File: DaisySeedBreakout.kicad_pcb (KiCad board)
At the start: 4 copper layers, 39.3 x 60.7 mm, 107 parts, among them J1 Conn_01x03, J10 Conn_01x03, J11 Conn_01x02, J12 Conn_01x02, J13 Conn_01x02, J14 Conn_01x03, J15 USB_B_Micro, J16 Conn_01x02, J17 Conn_01x02, J18 Conn_02x04, J19 Conn_01x06, J2 Conn_01x02, J20 Conn_01x04, J21 Conn_02x04, J23 Pins_02x10_P2.54mm_TH, J24 Conn_01x10, J25 Conn_01x02, J26 Conn_01x02, J3 Conn_01x03, J4 5027740891, J5 Conn_01x04, J6 Conn_01x02, J7 Conn_01x04, J8 Conn_01x02, J9 Conn_01x02, U1 H11L1M, U10 TPD2EUSB30ADRTR, U2 MAX4466EXK_T, U7 TLV9062IDR

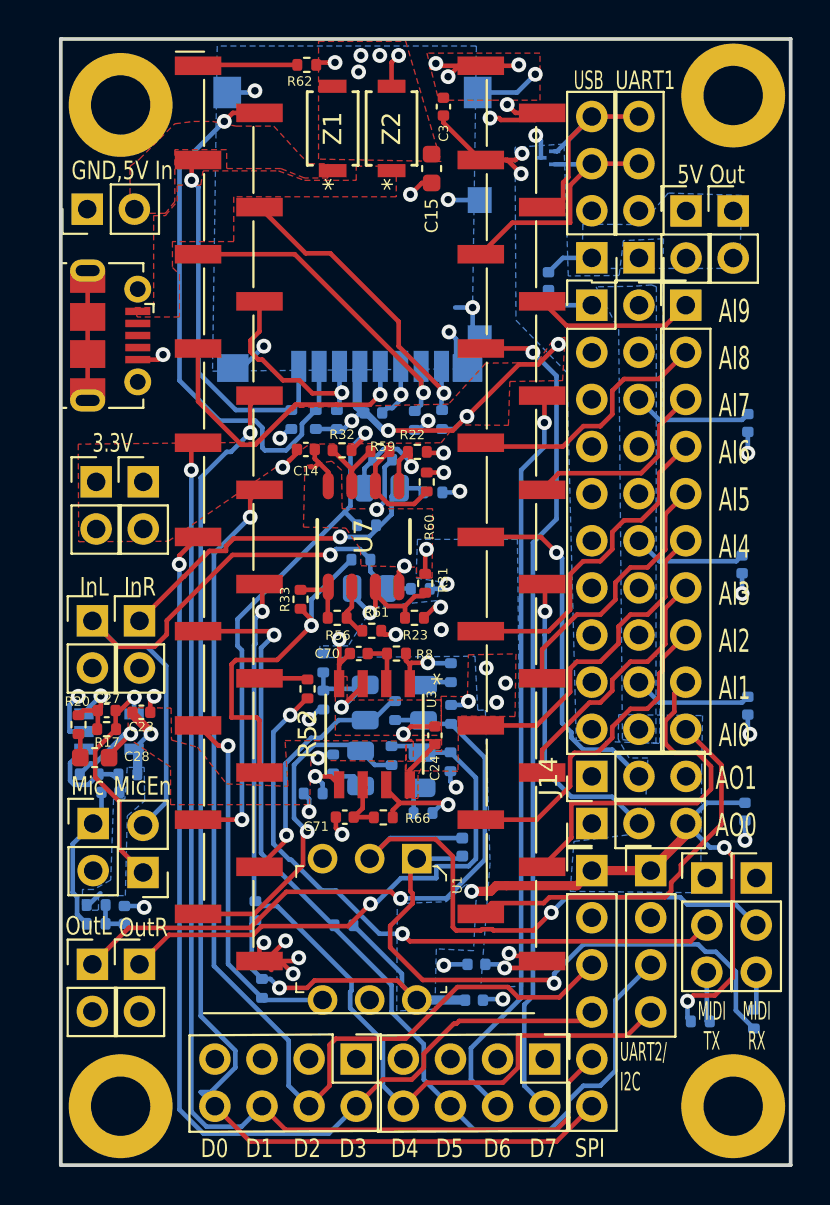
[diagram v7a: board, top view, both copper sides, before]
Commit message: PCB cleanup, added accelerometer as easy sensor to begin with
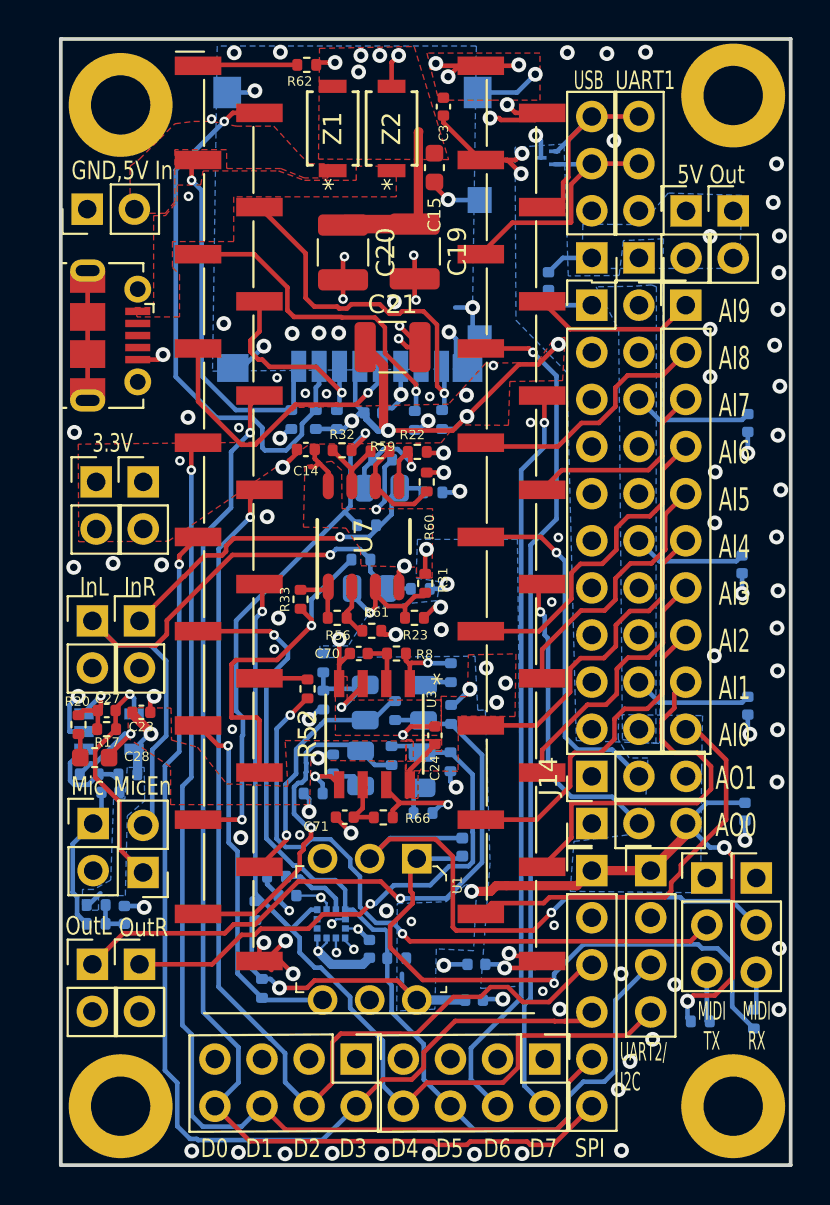
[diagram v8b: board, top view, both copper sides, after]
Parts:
- added C18: 0.1uF, Capacitor_SMD:C_0402_1005Metric, B.Cu at (141.1, 78.2)
- added C19: 100uF, Capacitor_SMD:C_1210_3225Metric, F.Cu at (147.9, 43.5)
- added C20: DNP_100uF, Capacitor_SMD:C_1210_3225Metric, F.Cu at (144.1, 43.5)
- added C21: DNP_100uF, Capacitor_SMD:C_1210_3225Metric, F.Cu at (146.7, 48.6)
- added C22: 0.1uF, Capacitor_SMD:C_0402_1005Metric, B.Cu at (145.5, 81.1)
- added R34: DNP, Resistor_SMD:R_0402_1005Metric, B.Cu at (140.5, 77.2)
- added U4: LIS2DE12, Package_LGA:LGA-12_2x2mm_P0.5mm, B.Cu at (143.4, 79.7)
- moved R6 3.35 mm to (147.0, 81.6)
- moved C15 0.16 mm to (149.0, 38.9)
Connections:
- net /Audio In/AUDIO_IN_L_CONN renamed /Audio_IN_L_CONN
- net /Audio In/AUDIO_IN_L_SUMMED renamed /Audio_IN_1
- net /Audio In/AUDIO_IN_R_CONN renamed /Audio_IN_R_CONN
- net /Audio In/AUDIO_IN_R_SUMMED renamed /Audio_IN_2
- net /Audio Out/AUDIO_OUT_L renamed /Audio_OUT_1
- net /Audio Out/AUDIO_OUT_L_EXT renamed /Audio_OUT_L_CONN
- net /Audio Out/AUDIO_OUT_R renamed /Audio_OUT_2
- net /Audio Out/AUDIO_OUT_R_EXT renamed /Audio_OUT_R_CONN
- net /Condensor Microphone/AUDIO_OUT renamed /Mic_OUT
- net /microSD/CLK renamed /SD_CLK
- net /microSD/CMD renamed /SD_CMD
- net /microSD/D0 renamed /SD_D0
- net /microSD/D1 renamed /SD_D1
- net /microSD/D2 renamed /SD_D2
- net /microSD/D3 renamed /SD_D3
- net Net-(C25-Pad1) renamed /Condensor Microphone/MIC_BIAS
- net Net-(C26-Pad2) renamed /Condensor Microphone/MIC_IN+
- net Net-(C27-Pad1) renamed /Condensor Microphone/MIC_IN-
- net Net-(D1-A) renamed /MIDI_IN_CONN
- net Net-(D1-K) renamed /MIDI_IN_Diode
- net Net-(J1-Pin_2) renamed /MIDI_TX_CONN
- net Net-(J1-Pin_3) renamed /MIDI_TX_PWR
- net Net-(J15-VBUS) renamed /USB_5V
- net Net-(J17-Pin_1) renamed /Condensor Microphone/MIC_CONN
- net Net-(J3-Pin_3) renamed /MIDI_IN_CONN_R
- net Net-(J6-Pin_2) renamed /HEADER_5V
- net Net-(R18-Pad1) renamed /Audio Out/L_out
- net Net-(R19-Pad1) renamed /Audio Out/R_out
- net Net-(U3A-+IN_A) renamed /Audio Out/L_in+
- net Net-(U3A--A) renamed /Audio Out/L_in-
- net Net-(U3B-+IN_B) renamed /Audio Out/R_in+
- net Net-(U3B--B) renamed /Audio Out/R_in-
- net Net-(U7A-IN+) renamed /Audio In/L_in+
- net Net-(U7A-IN-) renamed /Audio In/L_in-
- net Net-(U7A-OUT) renamed /Audio In/L_out+
- net Net-(U7B-IN+) renamed /Audio In/R_in+
- net Net-(U7B-IN-) renamed /Audio In/R_in-
- net Net-(U7B-OUT) renamed /Audio In/R_out+
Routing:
- net GND: track 82.0 -> 94.2 mm, vias 44 -> 130
- net +5V: track 9.56 -> 18.5 mm
- net +3.3V: track 99.8 -> 108.6 mm, vias 12 -> 14
- net Net-(U4-SA0/SDO): track 0.00 -> 3.77 mm
- net /DIO4_SCL_RX: track 48.7 -> 51.7 mm
- net /SD_D1: track 17.3 -> 20.2 mm
- net /DIO5_SDA_TX: track 51.5 -> 53.9 mm
- net /DIO3_PICO: track 57.2 -> 58.8 mm
- net /MIDI_TX_CONN: track 34.5 -> 35.7 mm
- net /SD_D0: track 18.1 -> 19.1 mm
- net /DIO0_CS: track 63.8 -> 63.1 mm
- net /AI_0: track 21.4 -> 21.9 mm
- net /Audio_OUT_R_CONN: track 30.6 -> 30.1 mm
- net /DIO1_SCK: track 61.8 -> 62.3 mm
